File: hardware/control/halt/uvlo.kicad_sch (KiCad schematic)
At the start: 11 parts, among them Q1 2N7000, U3 74HC14, U7 LM311, U8 74HC14

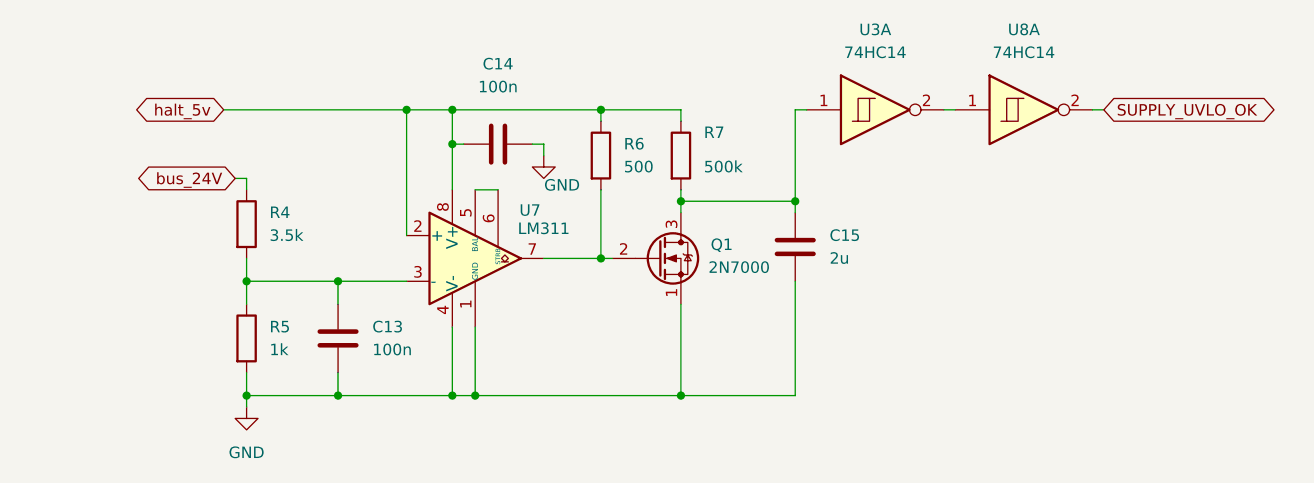
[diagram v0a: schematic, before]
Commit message: add progress on main drive controller and switch to hiearchical labels
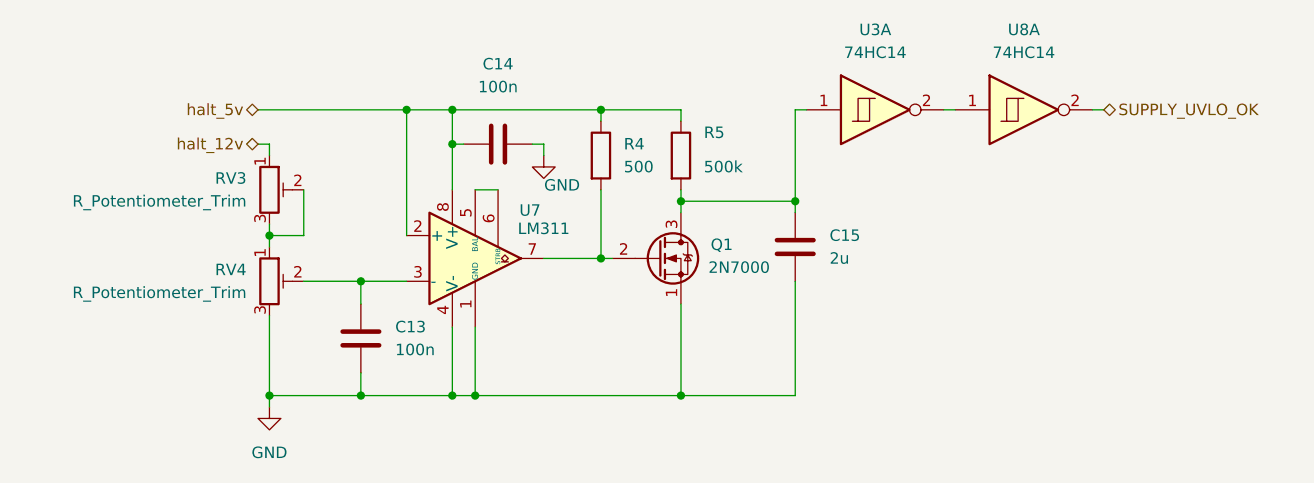
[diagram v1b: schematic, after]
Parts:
- removed R4: 3.5k, symbol Device:R
- removed R5: 1k, symbol Device:R
- added RV3, RV4: R_Potentiometer_Trim, symbol Device:R_Potentiometer_Trim
- renumbered R6 to R4, R7 to R5
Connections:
- net GND: now also RV4.3
- net at C13.1, U7.3 (-): now also RV4.2
- new net: RV3.2, RV3.3, RV4.1
- new net halt_12v: RV3.1
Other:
- moved on the sheet: C13

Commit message: update right about freaking everything
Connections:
- net halt_12v renamed bus_24V
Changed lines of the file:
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@@
 	)
 	(junction
-		(at 121.92 82.55)
+		(at 120.65 82.55)
 		(diameter 0)
 		(color 0 0 0 0)
@@
 	(wire
 		(pts
-			(xy 121.92 82.55) (xy 121.92 96.52)
+			(xy 120.65 82.55) (xy 120.65 96.52)
 		)
 		(stroke
@@
 	(wire
 		(pts
+			(xy 120.65 96.52) (xy 121.92 96.52)
+		)
+		(stroke
+			(width 0)
+			(type default)
+		)
+	)
+	(wire
+		(pts
 			(xy 110.49 96.52) (xy 106.68 96.52)
 		)
@@
 	(wire
 		(pts
-			(xy 105.41 82.55) (xy 121.92 82.55)
+			(xy 105.41 82.55) (xy 120.65 82.55)
 		)
 		(stroke
@@
 	(wire
 		(pts
-			(xy 129.54 91.44) (xy 132.08 91.44)
+			(xy 129.54 90.17) (xy 132.08 90.17)
 		)
 		(stroke
@@
 	(wire
 		(pts
+			(xy 106.68 96.52) (xy 106.68 97.79)
+		)
+		(stroke
+			(width 0)
+			(type default)
+		)
+	)
+	(wire
+		(pts
+			(xy 120.65 82.55) (xy 127 82.55)
+		)
+		(stroke
+			(width 0)
+			(type default)
+		)
+	)
+	(wire
+		(pts
+			(xy 132.08 90.17) (xy 132.08 91.44)
+		)
+		(stroke
+			(width 0)
+			(type default)
+		)
+	)
+	(wire
+		(pts
+			(xy 129.54 90.17) (xy 129.54 91.44)
+		)
+		(stroke
+			(width 0)
+			(type default)
+		)
+	)
+	(wire
+		(pts
+			(xy 129.54 114.3) (xy 129.54 106.68)
+		)
+		(stroke
+			(width 0)
+			(type default)
+		)
+	)
+	(wire
+		(pts
+			(xy 152.4 91.44) (xy 152.4 92.71)
+		)
+		(stroke
+			(width 0)
+			(type default)
+		)
+	)
+	(wire
+		(pts
+			(xy 165.1 101.6) (xy 165.1 114.3)
+		)
+		(stroke
+			(width 0)
+			(type default)
+		)
+	)
+	(wire
+		(pts
+			(xy 127 82.55) (xy 127 86.36)
+		)
+		(stroke
+			(width 0)
+			(type default)
+		)
+	)
+	(wire
+		(pts
+			(xy 165.1 92.71) (xy 165.1 93.98)
+		)
+		(stroke
+			(width 0)
+			(type default)
+		)
+	)
+	(wire
+		(pts
+			(xy 116.84 114.3) (xy 127 114.3)
+		)
+		(stroke
+			(width 0)
+			(type default)
+		)
+	)
+	(wire
+		(pts
+			(xy 137.16 86.36) (xy 135.89 86.36)
+		)
+		(stroke
+			(width 0)
+			(type default)
+		)
+	)
+	(wire
+		(pts
+			(xy 152.4 114.3) (xy 165.1 114.3)
+		)
+		(stroke
+			(width 0)
+			(type default)
+		)
+	)
+	(wire
+		(pts
+			(xy 116.84 111.76) (xy 116.84 114.3)
+		)
+		(stroke
+			(width 0)
+			(type default)
+		)
+	)
+	(wire
+		(pts
+			(xy 128.27 86.36) (xy 127 86.36)
+		)
+		(stroke
+			(width 0)
+			(type default)
+		)
+	)
+	(wire
+		(pts
+			(xy 106.68 114.3) (xy 106.68 115.57)
+		)
+		(stroke
+			(width 0)
+			(type default)
+		)
+	)
+	(wire
+		(pts
+			(xy 152.4 82.55) (xy 152.4 83.82)
+		)
+		(stroke
+			(width 0)
+			(type default)
+		)
+	)
+	(wire
+		(pts
 			(xy 105.41 86.36) (xy 106.68 86.36)
 		)
@@
 		)
 	)
-	(wire
-		(pts
-			(xy 106.68 96.52) (xy 106.68 97.79)
-		)
-		(stroke
-			(width 0)
-			(type default)
-		)
-	)
-	(wire
-		(pts
-			(xy 129.54 114.3) (xy 129.54 106.68)
-		)
-		(stroke
-			(width 0)
-			(type default)
-		)
-	)
-	(wire
-		(pts
-			(xy 152.4 91.44) (xy 152.4 92.71)
-		)
-		(stroke
-			(width 0)
-			(type default)
-		)
-	)
-	(wire
-		(pts
-			(xy 121.92 82.55) (xy 127 82.55)
-		)
-		(stroke
-			(width 0)
-			(type default)
-		)
-	)
-	(wire
-		(pts
-			(xy 165.1 101.6) (xy 165.1 114.3)
-		)
-		(stroke
-			(width 0)
-			(type default)
-		)
-	)
-	(wire
-		(pts
-			(xy 127 82.55) (xy 127 86.36)
-		)
-		(stroke
-			(width 0)
-			(type default)
-		)
-	)
-	(wire
-		(pts
-			(xy 165.1 92.71) (xy 165.1 93.98)
-		)
-		(stroke
-			(width 0)
-			(type default)
-		)
-	)
-	(wire
-		(pts
-			(xy 116.84 114.3) (xy 127 114.3)
-		)
-		(stroke
-			(width 0)
-			(type default)
-		)
-	)
-	(wire
-		(pts
-			(xy 137.16 86.36) (xy 135.89 86.36)
-		)
-		(stroke
-			(width 0)
-			(type default)
-		)
-	)
-	(wire
-		(pts
-			(xy 152.4 114.3) (xy 165.1 114.3)
-		)
-		(stroke
-			(width 0)
-			(type default)
-		)
-	)
-	(wire
-		(pts
-			(xy 116.84 111.76) (xy 116.84 114.3)
-		)
-		(stroke
-			(width 0)
-			(type default)
-		)
-	)
-	(wire
-		(pts
-			(xy 128.27 86.36) (xy 127 86.36)
-		)
-		(stroke
-			(width 0)
-			(type default)
-		)
-	)
-	(wire
-		(pts
-			(xy 106.68 114.3) (xy 106.68 115.57)
-		)
-		(stroke
-			(width 0)
-			(type default)
-		)
-	)
-	(wire
-		(pts
-			(xy 152.4 82.55) (xy 152.4 83.82)
-		)
-		(stroke
-			(width 0)
-			(type default)
+	(global_label "bus_24V"
+		(shape bidirectional)
+		(at 105.41 86.36 180)
+		(fields_autoplaced yes)
+		(effects
+			(font
+				(size 1.27 1.27)
+			)
+			(justify right)
+		)
+		(property "Intersheetrefs" "${INTERSHEET_REFS}"
+			(at 93.5122 86.36 0)
+			(effects
+				(font
+					(size 1.27 1.27)
+				)
+				(justify right)
+				(hide yes)
+			)
 		)
 	)
@@
 		(effects
 			(font
-				(size 1.27 1.27)
-			)
-			(justify right)
-		)
-	)
-	(hierarchical_label "halt_12v"
-		(shape bidirectional)
-		(at 105.41 86.36 180)
-		(effects
-			(font
